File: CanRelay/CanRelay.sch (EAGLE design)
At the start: 19 parts

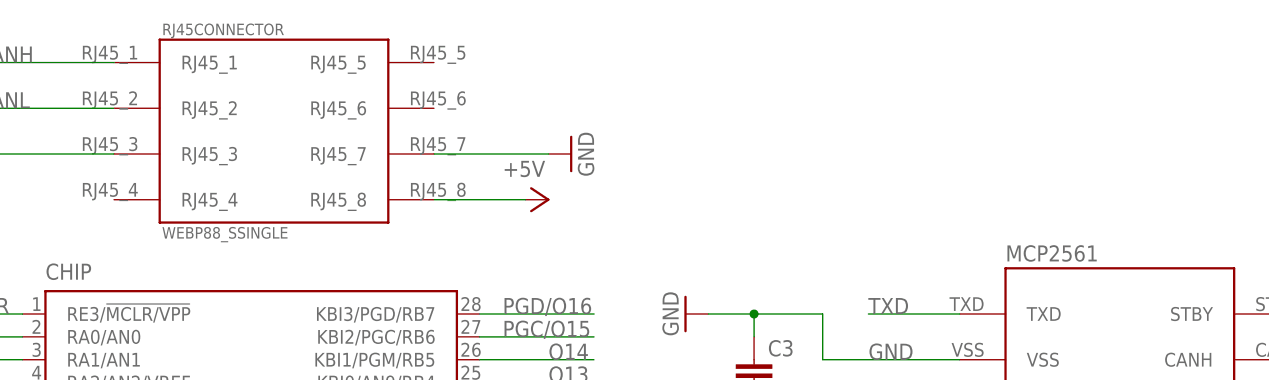
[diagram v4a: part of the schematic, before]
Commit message: #5 adding last missing component - power jack - to the schema only. And added all wiring, ready to generate the board now
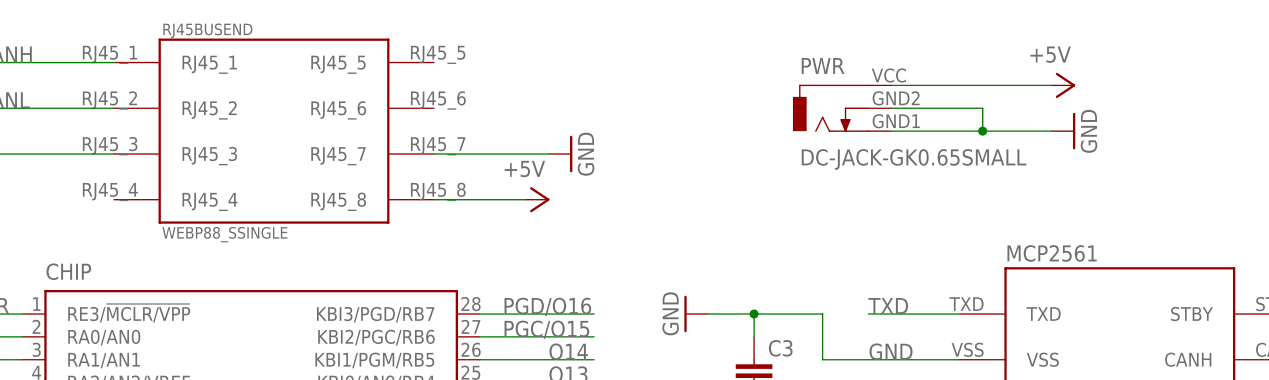
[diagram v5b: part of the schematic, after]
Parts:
- added PWR: DC-JACK-GK0.65SMALL, PoJD:DC-JACK-GK0.65SMALL
- renumbered RJ45CONNECTOR to RJ45BUSEND
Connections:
- net +5V: now also PWR.VCC
- net GND: now also PWR.GND1, PWR.GND2
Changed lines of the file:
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@@
 <part name="GND1" library="supply1" deviceset="GND" device=""/>
 <part name="OUTPUTS" library="pinhead" deviceset="PINHD-2X10" device=""/>
-<part name="RJ45CONNECTOR" library="PoJD" deviceset="WEBP88_S" device="SINGLE"/>
+<part name="RJ45BUSEND" library="PoJD" deviceset="WEBP88_S" device="SINGLE"/>
 <part name="P+4" library="supply1" deviceset="+5V" device=""/>
 <part name="GND7" library="supply1" deviceset="GND" device=""/>
 <part name="GND8" library="supply1" deviceset="GND" device=""/>
 <part name="USBTIN" library="PoJD" deviceset="ARK350/3" device="STANDARD"/>
+<part name="PWR" library="PoJD" deviceset="DC-JACK-GK0.65" device="SMALL"/>
+<part name="GND9" library="supply1" deviceset="GND" device=""/>
+<part name="P+5" library="supply1" deviceset="+5V" device=""/>
 </parts>
 <sheets>
@@
 <instance part="GND1" gate="1" x="63.5" y="63.5" rot="R90"/>
 <instance part="OUTPUTS" gate="A" x="-93.98" y="45.72"/>
-<instance part="RJ45CONNECTOR" gate="G$1" x="-73.66" y="124.46"/>
+<instance part="RJ45BUSEND" gate="G$1" x="-73.66" y="124.46"/>
 <instance part="P+4" gate="1" x="-43.18" y="116.84" rot="R270"/>
 <instance part="GND7" gate="1" x="-40.64" y="121.92" rot="R90"/>
 <instance part="GND8" gate="1" x="-106.68" y="121.92" rot="R270"/>
 <instance part="USBTIN" gate="G$1" x="15.24" y="45.72"/>
+<instance part="PWR" gate="G$1" x="-12.7" y="127"/>
+<instance part="GND9" gate="1" x="15.24" y="124.46" rot="R90"/>
+<instance part="P+5" gate="1" x="15.24" y="129.54" rot="R270"/>
 </instances>
 <busses>
@@
 </segment>
 <segment>
-<pinref part="RJ45CONNECTOR" gate="G$1" pin="RJ45_8"/>
+<pinref part="RJ45BUSEND" gate="G$1" pin="RJ45_8"/>
 <pinref part="P+4" gate="1" pin="+5V"/>
 <wire x1="-55.88" y1="116.84" x2="-45.72" y2="116.84" width="0.1524" layer="91"/>
+</segment>
+<segment>
+<pinref part="PWR" gate="G$1" pin="VCC"/>
+<pinref part="P+5" gate="1" pin="+5V"/>
+<wire x1="-5.08" y1="129.54" x2="12.7" y2="129.54" width="0.1524" layer="91"/>
 </segment>
 </net>
@@
 </segment>
 <segment>
-<pinref part="RJ45CONNECTOR" gate="G$1" pin="RJ45_7"/>
+<pinref part="RJ45BUSEND" gate="G$1" pin="RJ45_7"/>
 <pinref part="GND7" gate="1" pin="GND"/>
 <wire x1="-55.88" y1="121.92" x2="-43.18" y2="121.92" width="0.1524" layer="91"/>
 </segment>
 <segment>
-<pinref part="RJ45CONNECTOR" gate="G$1" pin="RJ45_3"/>
+<pinref part="RJ45BUSEND" gate="G$1" pin="RJ45_3"/>
 <pinref part="GND8" gate="1" pin="GND"/>
 <wire x1="-91.44" y1="121.92" x2="-104.14" y2="121.92" width="0.1524" layer="91"/>
@@
 <wire x1="12.7" y1="38.1" x2="-2.54" y2="38.1" width="0.1524" layer="91"/>
 <label x="-2.54" y="38.1" size="1.778" layer="95"/>
+</segment>
+<segment>
+<pinref part="PWR" gate="G$1" pin="GND1"/>
+<pinref part="GND9" gate="1" pin="GND"/>
+<wire x1="-5.08" y1="124.46" x2="5.08" y2="124.46" width="0.1524" layer="91"/>
+<pinref part="PWR" gate="G$1" pin="GND2"/>
+<wire x1="5.08" y1="124.46" x2="12.7" y2="124.46" width="0.1524" layer="91"/>
+<wire x1="-5.08" y1="127" x2="5.08" y2="127" width="0.1524" layer="91"/>
+<wire x1="5.08" y1="127" x2="5.08" y2="124.46" width="0.1524" layer="91"/>
+<junction x="5.08" y="124.46"/>
 </segment>
 </net>
@@
 </segment>
 <segment>
-<pinref part="RJ45CONNECTOR" gate="G$1" pin="RJ45_1"/>
+<pinref part="RJ45BUSEND" gate="G$1" pin="RJ45_1"/>
 <wire x1="-91.44" y1="132.08" x2="-106.68" y2="132.08" width="0.1524" layer="91"/>
 <label x="-106.68" y="132.08" size="1.778" layer="95"/>
@@
 </segment>
 <segment>
-<pinref part="RJ45CONNECTOR" gate="G$1" pin="RJ45_2"/>
+<pinref part="RJ45BUSEND" gate="G$1" pin="RJ45_2"/>
 <wire x1="-91.44" y1="127" x2="-106.68" y2="127" width="0.1524" layer="91"/>
 <label x="-106.68" y="127" size="1.778" layer="95"/>

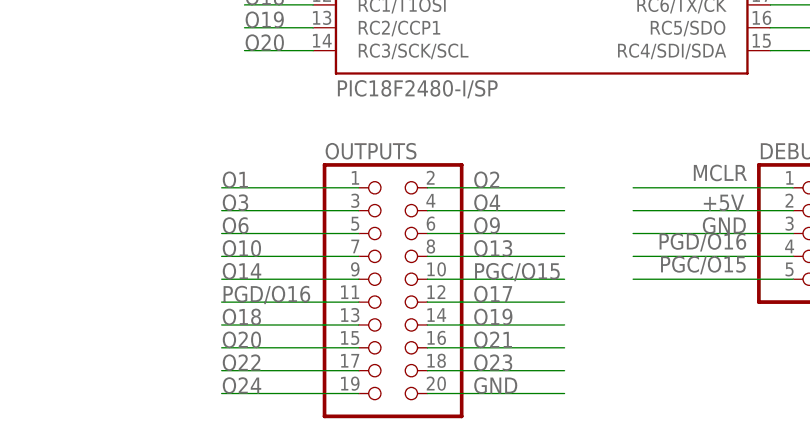
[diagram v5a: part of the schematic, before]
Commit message: first draft version of the board with routed everything and copper ground too
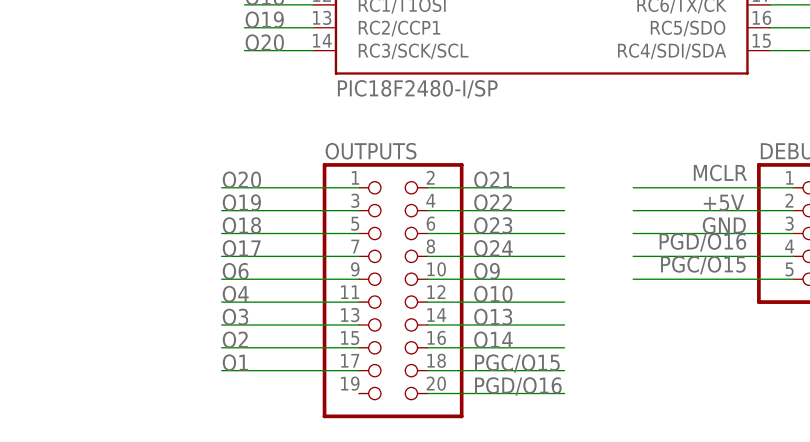
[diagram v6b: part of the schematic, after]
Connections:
- net GND: no longer OUTPUTS.20
- net O1: now also OUTPUTS.17; no longer OUTPUTS.1
- net O10: now also OUTPUTS.12; no longer OUTPUTS.7
- net O13: now also OUTPUTS.14; no longer OUTPUTS.8
- net O14: now also OUTPUTS.16; no longer OUTPUTS.9
- net O17: now also OUTPUTS.7; no longer OUTPUTS.12
- net O18: now also OUTPUTS.5; no longer OUTPUTS.13
- net O19: now also OUTPUTS.3; no longer OUTPUTS.14
- net O2: now also OUTPUTS.15; no longer OUTPUTS.2
- net O20: now also OUTPUTS.1; no longer OUTPUTS.15
- net O21: now also OUTPUTS.2; no longer OUTPUTS.16
- net O22: now also OUTPUTS.4; no longer OUTPUTS.17
- net O23: now also OUTPUTS.6; no longer OUTPUTS.18
- net O24: now also OUTPUTS.8; no longer OUTPUTS.19
- net O3: now also OUTPUTS.13; no longer OUTPUTS.3
- net O4: now also OUTPUTS.11; no longer OUTPUTS.4
- net O6: now also OUTPUTS.9; no longer OUTPUTS.5
- net O9: now also OUTPUTS.10; no longer OUTPUTS.6
- net PGC/O15: now also OUTPUTS.18; no longer OUTPUTS.10
- net PGD/O16: now also OUTPUTS.20; no longer OUTPUTS.11

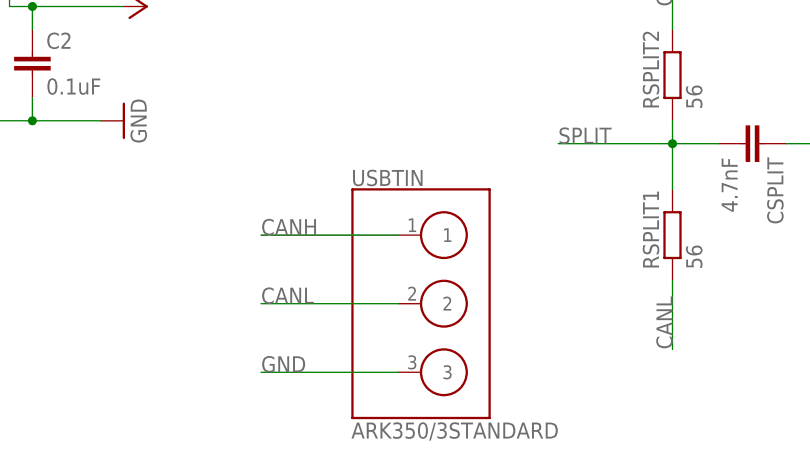
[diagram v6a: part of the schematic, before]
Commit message: positioned all components nicely on the board and redid all wires thoroughly this time. Also replaced 3pin for usbtin by regular pinhead since that would be easier to plug into the board
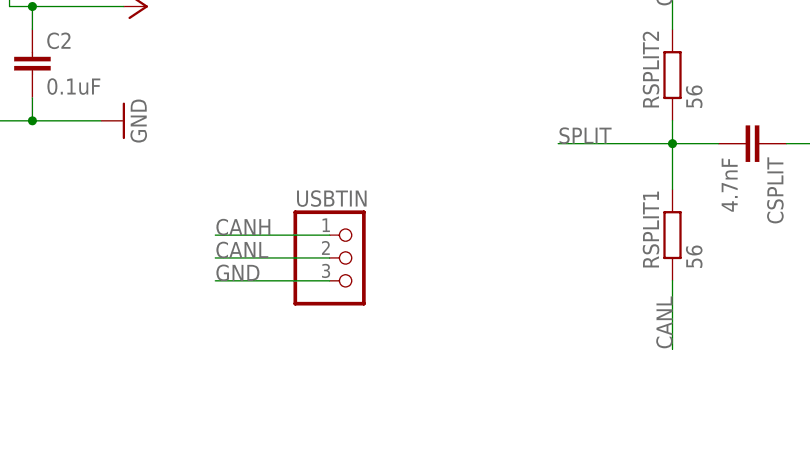
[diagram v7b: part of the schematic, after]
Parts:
- USBTIN: value ARK350/3STANDARD -> (none); device PoJD:ARK350/3STANDARD -> pinhead:PINHD-1X3
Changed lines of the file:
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@@
 <part name="GND7" library="supply1" deviceset="GND" device=""/>
 <part name="GND8" library="supply1" deviceset="GND" device=""/>
-<part name="USBTIN" library="PoJD" deviceset="ARK350/3" device="STANDARD"/>
 <part name="PWR" library="PoJD" deviceset="DC-JACK-GK0.65" device="SMALL"/>
 <part name="GND9" library="supply1" deviceset="GND" device=""/>
 <part name="P+5" library="supply1" deviceset="+5V" device=""/>
+<part name="USBTIN" library="pinhead" deviceset="PINHD-1X3" device=""/>
 </parts>
 <sheets>
@@
 <instance part="GND7" gate="1" x="-40.64" y="121.92" rot="R90"/>
 <instance part="GND8" gate="1" x="-106.68" y="121.92" rot="R270"/>
-<instance part="USBTIN" gate="G$1" x="15.24" y="45.72"/>
 <instance part="PWR" gate="G$1" x="-12.7" y="127"/>
 <instance part="GND9" gate="1" x="15.24" y="124.46" rot="R90"/>
 <instance part="P+5" gate="1" x="15.24" y="129.54" rot="R270"/>
+<instance part="USBTIN" gate="A" x="7.62" y="50.8"/>
 </instances>
 <busses>
@@
 </segment>
 <segment>
-<pinref part="USBTIN" gate="G$1" pin="3"/>
-<wire x1="12.7" y1="38.1" x2="-2.54" y2="38.1" width="0.1524" layer="91"/>
-<label x="-2.54" y="38.1" size="1.778" layer="95"/>
-</segment>
-<segment>
 <pinref part="PWR" gate="G$1" pin="GND1"/>
 <pinref part="GND9" gate="1" pin="GND"/>
@@
 <wire x1="5.08" y1="127" x2="5.08" y2="124.46" width="0.1524" layer="91"/>
 <junction x="5.08" y="124.46"/>
+</segment>
+<segment>
+<pinref part="USBTIN" gate="A" pin="3"/>
+<wire x1="5.08" y1="48.26" x2="-7.62" y2="48.26" width="0.1524" layer="91"/>
+<label x="-7.62" y="48.26" size="1.778" layer="95"/>
 </segment>
 </net>
@@
 </segment>
 <segment>
-<pinref part="USBTIN" gate="G$1" pin="1"/>
-<wire x1="12.7" y1="53.34" x2="-2.54" y2="53.34" width="0.1524" layer="91"/>
-<label x="-2.54" y="53.34" size="1.778" layer="95"/>
+<pinref part="USBTIN" gate="A" pin="1"/>
+<wire x1="5.08" y1="53.34" x2="-7.62" y2="53.34" width="0.1524" layer="91"/>
+<label x="-7.62" y="53.34" size="1.778" layer="95"/>
 </segment>
 </net>
@@
 </segment>
 <segment>
-<pinref part="USBTIN" gate="G$1" pin="2"/>
-<wire x1="12.7" y1="45.72" x2="-2.54" y2="45.72" width="0.1524" layer="91"/>
-<label x="-2.54" y="45.72" size="1.778" layer="95"/>
-</segment>
-</net>
+<pinref part="USBTIN" gate="A" pin="2"/>
+<wire x1="5.08" y1="50.8" x2="-7.62" y2="50.8" width="0.1524" layer="91"/>
+<label x="-7.62" y="50.8" size="1.778" layer="95"/>
+</segment>
+</net>

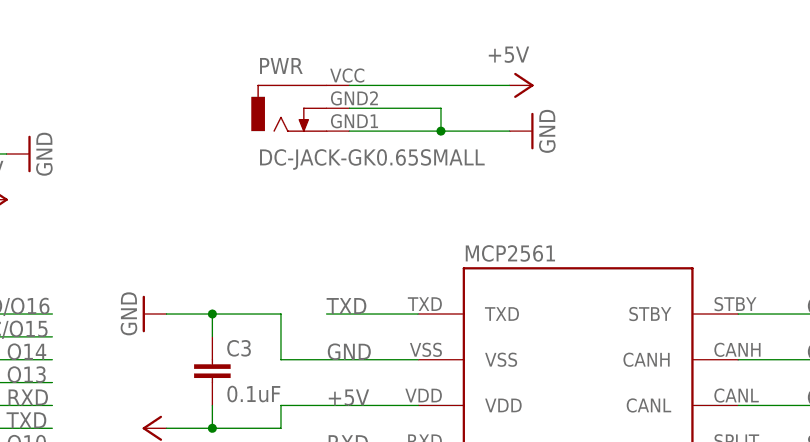
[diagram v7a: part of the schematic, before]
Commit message: final tuning of both boards - squeezing switch board a bit yet, adding some more silkscreen, exporting to image to share on some electrical forums for checks
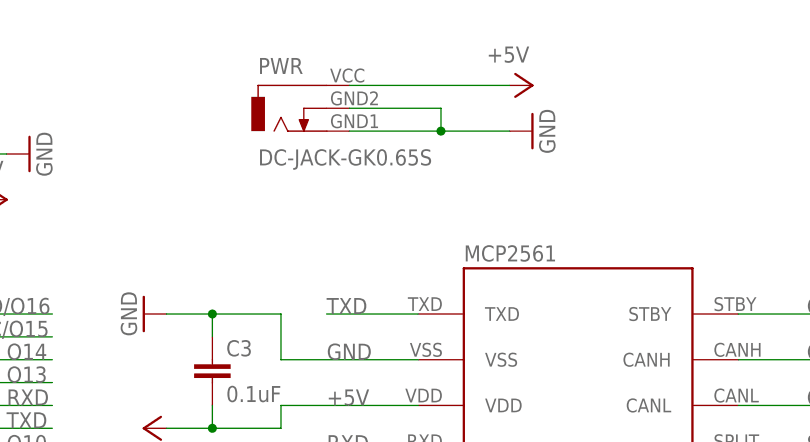
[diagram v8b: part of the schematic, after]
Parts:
- PWR: value DC-JACK-GK0.65SMALL -> DC-JACK-GK0.65S; device PoJD:DC-JACK-GK0.65SMALL -> PoJD:DC-JACK-GK0.65S
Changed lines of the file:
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@@
 <part name="GND7" library="supply1" deviceset="GND" device=""/>
 <part name="GND8" library="supply1" deviceset="GND" device=""/>
-<part name="PWR" library="PoJD" deviceset="DC-JACK-GK0.65" device="SMALL"/>
+<part name="PWR" library="PoJD" deviceset="DC-JACK-GK0.65" device="S"/>
 <part name="GND9" library="supply1" deviceset="GND" device=""/>
 <part name="P+5" library="supply1" deviceset="+5V" device=""/>
